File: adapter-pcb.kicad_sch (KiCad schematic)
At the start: 0 parts

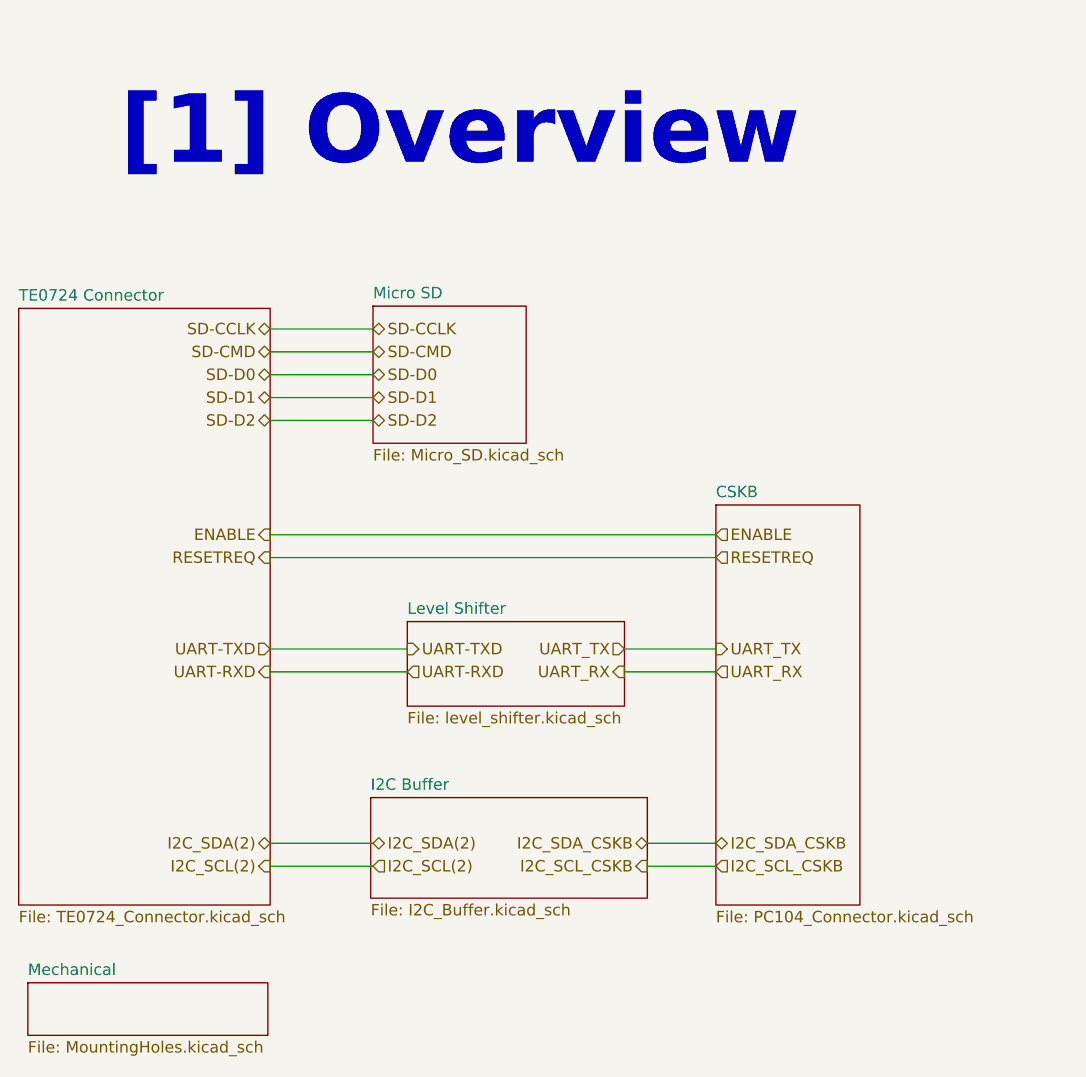
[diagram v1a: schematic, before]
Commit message: Added Level Shifter for SD card
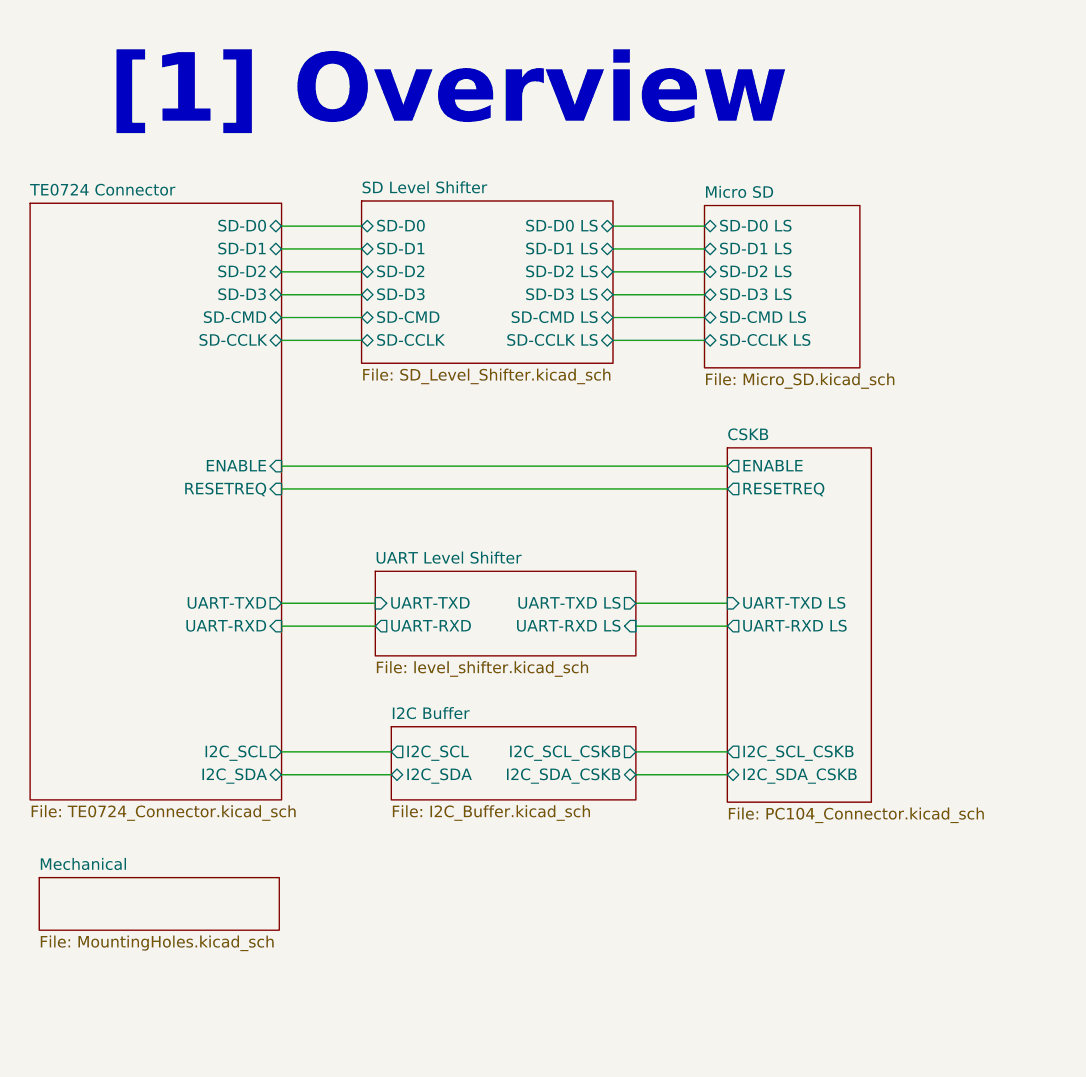
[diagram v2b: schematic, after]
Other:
- sheet Level Shifter renamed UART Level Shifter
- added sheet SD Level Shifter (SD_Level_Shifter.kicad_sch)
- sheet CSKB ports: added ENABLE, I2C_SCL_CSKB, I2C_SDA_CSKB, RESETREQ, UART-RXD LS, UART-TXD LS; removed none
- sheet I2C Buffer ports: added I2C_SCL, I2C_SCL_CSKB, I2C_SDA, I2C_SDA_CSKB; removed none
- sheet Micro SD ports: added SD-CCLK LS, SD-CMD LS, SD-D0 LS, SD-D1 LS, SD-D2 LS, SD-D3 LS; removed none
- sheet TE0724 Connector ports: added ENABLE, I2C_SCL, I2C_SDA, RESETREQ, SD-CCLK, SD-CMD, SD-D0, SD-D1, SD-D2, SD-D3, UART-RXD, UART-TXD; removed none
- sheet UART Level Shifter ports: added UART-RXD, UART-RXD LS, UART-TXD, UART-TXD LS; removed none

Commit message: Changed connector orientation and power changes
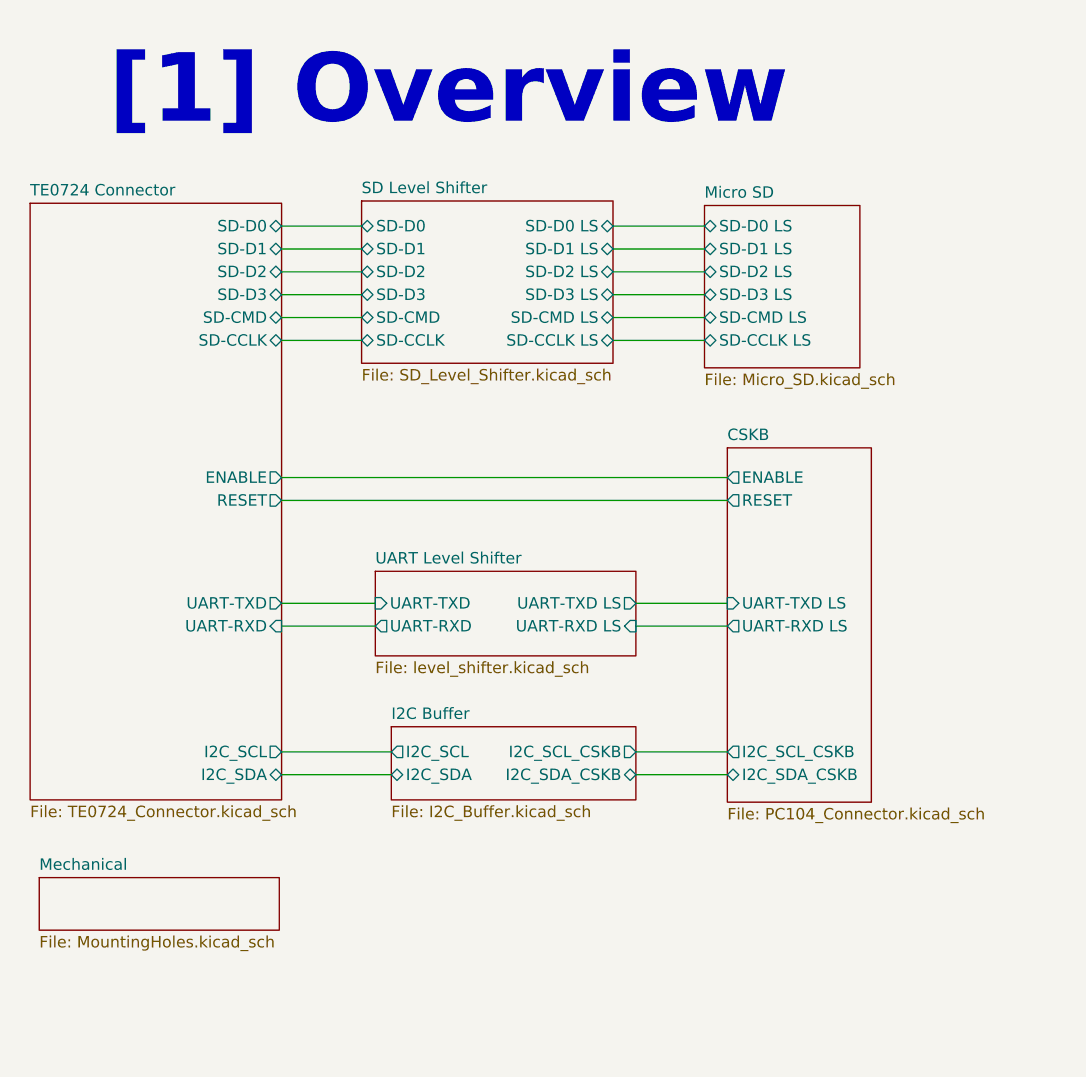
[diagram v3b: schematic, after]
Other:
- sheet CSKB ports: added RESET; removed RESETREQ
- sheet TE0724 Connector ports: added RESET; removed RESETREQ
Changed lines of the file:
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@@
-	(wire
-		(pts
-			(xy 127 64.77) (xy 176.53 64.77)
-		)
-		(stroke
-			(width 0)
-			(type default)
-		)
-	)
 	(wire
 		(pts
@@
 	(wire
 		(pts
-			(xy 127 67.31) (xy 176.53 67.31)
-		)
-		(stroke
-			(width 0)
-			(type default)
-		)
-	)
-	(wire
-		(pts
 			(xy 127 48.26) (xy 135.89 48.26)
 		)
@@
 	(wire
 		(pts
+			(xy 127 66.04) (xy 176.53 66.04)
+		)
+		(stroke
+			(width 0)
+			(type default)
+		)
+	)
+	(wire
+		(pts
 			(xy 166.37 99.06) (xy 176.53 99.06)
 		)
@@
 		(pts
 			(xy 127 82.55) (xy 137.414 82.55)
+		)
+		(stroke
+			(width 0)
+			(type default)
+		)
+	)
+	(wire
+		(pts
+			(xy 127 68.58) (xy 176.53 68.58)
 		)
 		(stroke
@@
 			)
 		)
-		(pin "RESETREQ" input
-			(at 127 67.31 0)
-			(effects
-				(font
-					(size 1.27 1.27)
-				)
-				(justify right)
-			)
-		)
-		(pin "ENABLE" input
-			(at 127 64.77 0)
-			(effects
-				(font
-					(size 1.27 1.27)
-				)
-				(justify right)
-			)
-		)
 		(pin "SD-D2" bidirectional
 			(at 127 43.18 0)
@@
 		(pin "UART-RXD" input
 			(at 127 82.55 0)
+			(effects
+				(font
+					(size 1.27 1.27)
+				)
+				(justify right)
+			)
+		)
+		(pin "ENABLE" output
+			(at 127 66.04 0)
+			(effects
+				(font
+					(size 1.27 1.27)
+				)
+				(justify right)
+			)
+		)
+		(pin "RESET" output
+			(at 127 68.58 0)
 			(effects
 				(font
@@
 			)
 		)
-		(pin "ENABLE" output
-			(at 176.53 64.77 180)
-			(effects
-				(font
-					(size 1.27 1.27)
-				)
-				(justify left)
-			)
-		)
 		(pin "I2C_SCL_CSKB" output
 			(at 176.53 96.52 180)
@@
 			)
 		)
-		(pin "RESETREQ" output
-			(at 176.53 67.31 180)
-			(effects
-				(font
-					(size 1.27 1.27)
-				)
-				(justify left)
-			)
-		)
 		(pin "UART-RXD LS" output
 			(at 176.53 82.55 180)
@@
 			(effects
 				(font
+					(size 1.27 1.27)
+				)
+				(justify left)
+			)
+		)
+		(pin "ENABLE" output
+			(at 176.53 66.04 180)
+			(effects
+				(font
+					(size 1.27 1.27)
+				)
+				(justify left)
+			)
+		)
+		(pin "RESET" output
+			(at 176.53 68.58 180)
+			(effects
+				(font
